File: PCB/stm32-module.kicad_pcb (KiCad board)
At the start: 4 copper layers, 70.2 x 87.4 mm, 24 parts, among them J1 Left, J2 Right

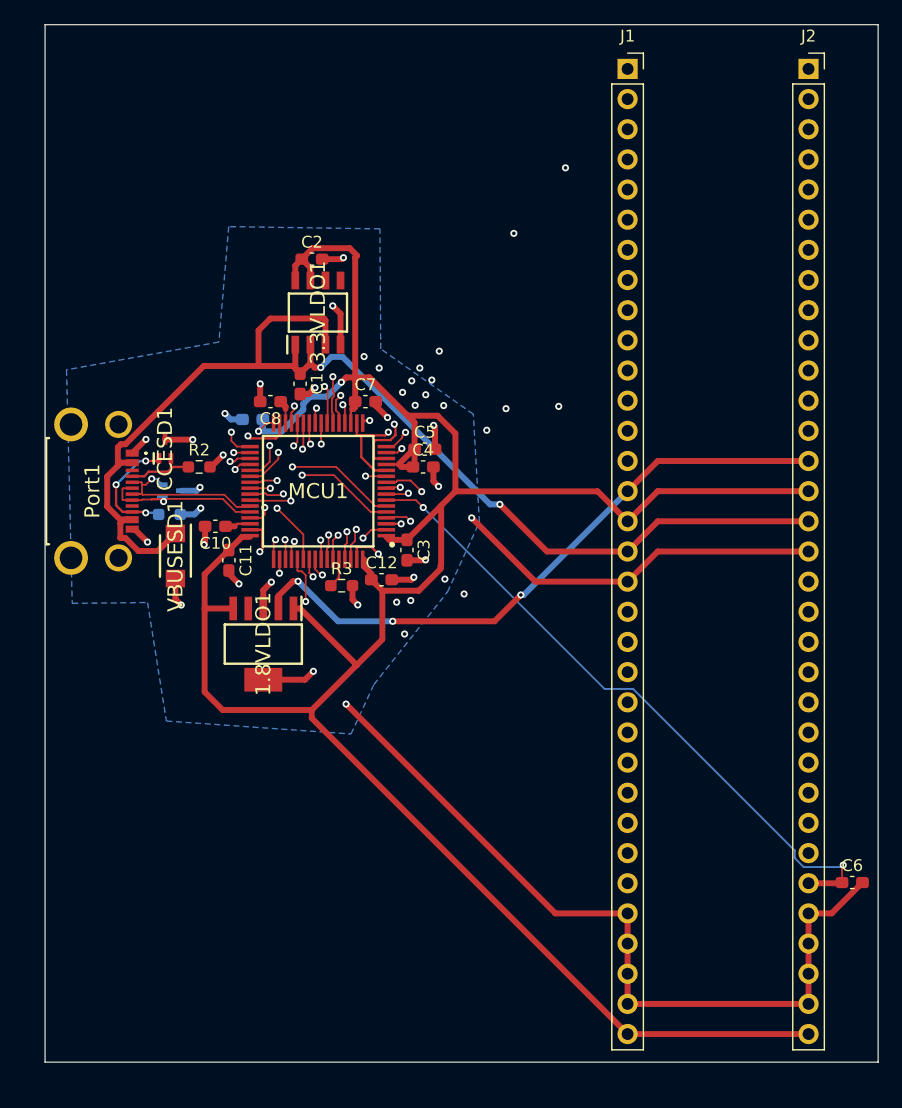
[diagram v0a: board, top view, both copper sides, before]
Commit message: Added images to rom, also rerouted everything
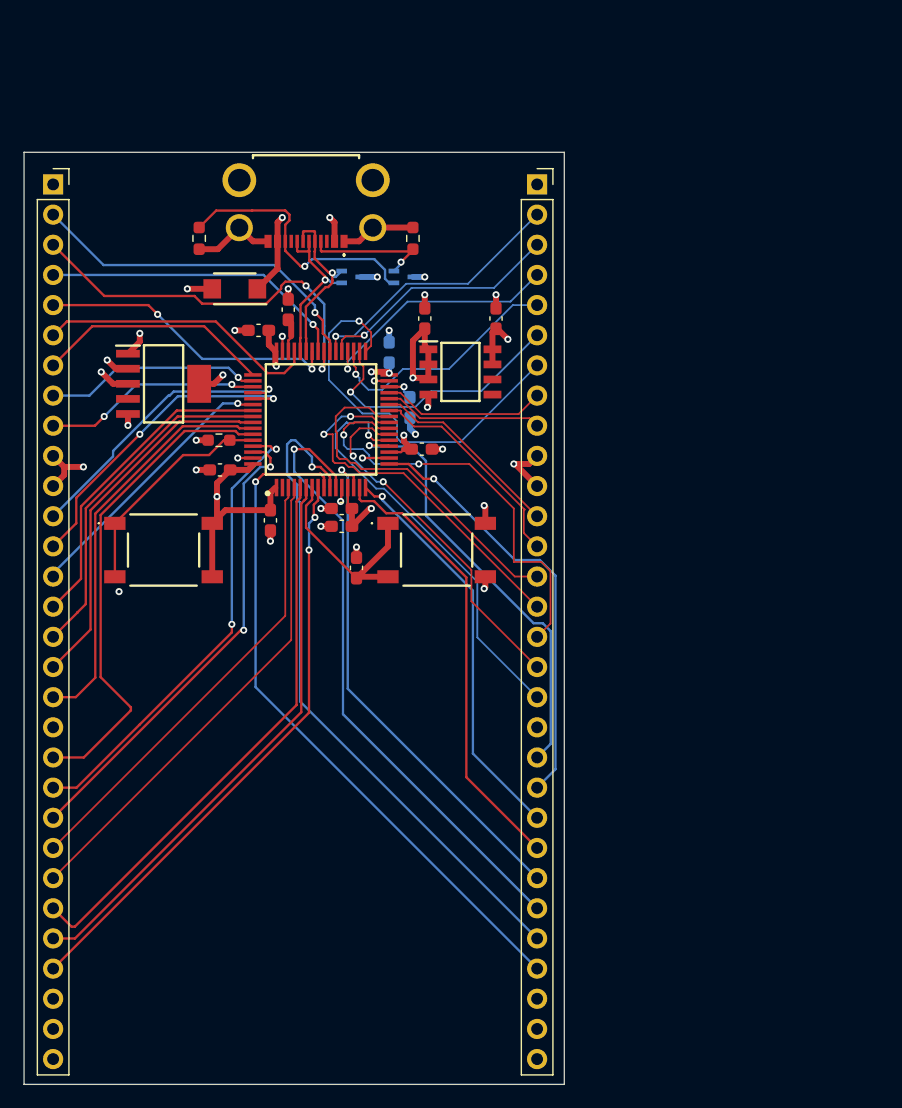
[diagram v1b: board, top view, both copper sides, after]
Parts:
- added S1: TS40-66-43-BK-160-SMT-TR, REQUIRED:TS406643BK160SMTTR, F.Cu at (116.0, 71.0)
- added S2: TS40-66-43-BK-160-SMT-TR, REQUIRED:TS406643BK160SMTTR, F.Cu at (93.0, 71.0)
- 1.8VLDO1: footprint SamacSys_Parts:SOT127P706X180-6N -> REQUIRED:SOT127P706X180-6N
- 3.3VLDO1: footprint SamacSys_Parts:SOIC127P600X175-8N -> REQUIRED:SOIC127P600X175-8N
- C1, C10, C11, C12, C2, C3, C4, C5, C6, C7, C9: footprint Capacitor_SMD:C_0603_1608Metric_Pad1.08x0.95mm_HandSolder -> REQUIRED:C_0603_1608Metric_Pad1.08x0.95mm_HandSolder
- C8: footprint Capacitor_SMD:C_0603_1608Metric_Pad1.08x0.95mm_HandSolder -> REQUIRED:C_0603_1608Metric_Pad1.08x0.95mm_HandSolder; moved to B.Cu
- CCESD1: footprint SamacSys_Parts:SOT50P160X90-3N -> REQUIRED:SOT50P160X90-3N; moved to B.Cu
- DATAESD1: footprint SamacSys_Parts:SOT50P160X90-3N -> REQUIRED:SOT50P160X90-3N
- J1: value Left -> Conn_01x30_Socket; footprint Connector_PinSocket_2.54mm:PinSocket_1x33_P2.54mm_Vertical -> REQUIRED:PinSocket_1x30_P2.54mm_Vertical
- J2: value Right -> Conn_01x30_Socket; footprint Connector_PinSocket_2.54mm:PinSocket_1x33_P2.54mm_Vertical -> REQUIRED:PinSocket_1x30_P2.54mm_Vertical
- MCU1: footprint SamacSys_Parts:QFP50P1200X1200X160-64N -> REQUIRED:QFP50P1200X1200X160-64N
- Port1: footprint SamacSys_Parts:2169900003 -> REQUIRED:2169900003
- R1: footprint Resistor_SMD:R_0603_1608Metric_Pad0.98x0.95mm_HandSolder -> REQUIRED:R_0603_1608Metric_Pad0.98x0.95mm_HandSolder; moved to F.Cu
- R2, R3: footprint Resistor_SMD:R_0603_1608Metric_Pad0.98x0.95mm_HandSolder -> REQUIRED:R_0603_1608Metric_Pad0.98x0.95mm_HandSolder
- VBUSESD1: footprint SamacSys_Parts:SODFL4626X140N -> REQUIRED:SODFL4626X140N
- moved C6 49.5 mm to (109.2, 72.5), turned to 90 degrees
- moved J1 49.3 mm to (83.7, 40.2)
- moved Port1 31.2 mm to (105.0, 41.0), turned to 180 degrees
- moved R2 26.4 mm to (114.0, 44.8), turned to 90 degrees
- moved J2 24.8 mm to (124.5, 40.2)
- moved CCESD1 24.8 mm to (113.2, 48.0), turned to 0 degrees
- moved DATAESD1 23.5 mm to (108.8, 48.0)
- moved 1.8VLDO1 23.5 mm to (93.0, 57.0), turned to 0 degrees
- moved R1 23.4 mm to (96.0, 44.8), turned to -90 degrees
- moved VBUSESD1 23.0 mm to (99.0, 49.0), turned to 180 degrees
- moved C11 19.5 mm to (101.0, 52.5), turned to 180 degrees
- moved C10 19.3 mm to (103.5, 50.8), turned to 90 degrees
- moved C12 16.5 mm to (97.8, 64.2), turned to 180 degrees
- moved C2 16.3 mm to (121.0, 51.5), turned to 90 degrees
- moved R3 16.0 mm to (97.7, 61.8), turned to 180 degrees
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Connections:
- net Net-(MCU1-BOOT0) renamed /BOOT0
- J1 pad 1: /PA0 -> /VBUS
- J1 pad 10: /PA9 -> /1.8V
- J1 pad 11: /PA10 -> /1.8V
- J1 pad 12: /PA13 -> /PC11
- J1 pad 13: /PA14 -> /PC12
- J1 pad 14: /PA15 -> /PD2
- J1 pad 15: /1.8V -> /PB3
- J1 pad 16: /VDDA -> /PB4
- J1 pad 17: /VBUS -> /PB5
- J1 pad 18: GND -> /PB6
- J1 pad 19: /PB0 -> GND
- J1 pad 2: /PA1 -> /PC9
- J1 pad 20: /PB1 -> /PB7
- J1 pad 21: /PB2 -> /PB8
- J1 pad 22: /PB3 -> /PB9
- J1 pad 23: /PB4 -> /PC14
- J1 pad 24: /PB5 -> /PC15
- J1 pad 25: /PB6 -> /PH0
- J1 pad 26: /PB7 -> /PH1
- J1 pad 27: /PB8 -> /PC0
- J1 pad 28: /PB9 -> GND
- J1 pad 3: /PA2 -> /PA8
- J1 pad 4: /PA3 -> /PA9
- J1 pad 5: /PA4 -> /PA10
- J1 pad 6: /PA5 -> /PA13
- J1 pad 7: /PA6 -> /PA14
- J1 pad 8: /PA7 -> /PA15
- J1 pad 9: /PA8 -> /PC10
- J2 pad 1: /PB10 -> /VBUS
- J2 pad 10: /PC4 -> /VDDA
- J2 pad 11: /PC5 -> /VDDA
- J2 pad 12: /PC6 -> /PB1
- J2 pad 13: /PC7 -> /PB0
- J2 pad 14: /1.8V -> /PC5
- J2 pad 15: /VDDA -> /PC4
- J2 pad 16: /VBUS -> /PA7
- J2 pad 17: GND -> /PA6
- J2 pad 18: /PC9 -> /PA5
- J2 pad 19: /PC10 -> GND
- J2 pad 2: /PB12 -> /PC7
- J2 pad 20: /PC11 -> /PA4
- J2 pad 21: /PC12 -> /PA3
- J2 pad 22: /PC13 -> /PA2
- J2 pad 23: /PC14 -> /PA1
- J2 pad 24: /PC15 -> /PA0
- J2 pad 25: /PD2 -> /PC3
- J2 pad 26: /PH0 -> /PC2
- J2 pad 27: /PH1 -> /PC1
- J2 pad 28: /NRST -> GND
- J2 pad 3: /PB13 -> /PC6
- J2 pad 4: /PB14 -> /PB15
- J2 pad 5: /PB15 -> /PB14
- J2 pad 6: /PC0 -> /PB13
- J2 pad 7: /PC1 -> /PB12
- J2 pad 8: /PC2 -> /PB10
- J2 pad 9: /PC3 -> /PB2
- MCU1 pad 2: /PC13 -> unconnected-(MCU1-PC13-Pad2)
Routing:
- net /VDDA: track 215.1 -> 132.9 mm, vias 2 -> 10
- net /PB14: track 83.0 -> 20.9 mm
- net /PC7: track 82.3 -> 22.5 mm, vias 4 -> 1
- net /PB13: track 77.1 -> 22.8 mm
- net /PC6: track 70.8 -> 20.7 mm, vias 2 -> 1
- net /PC13: track 49.4 -> 0.00 mm, vias 2 -> 0
- net /PB10: track 58.0 -> 13.8 mm, vias 1 -> 0
- net /PD2: track 65.1 -> 23.1 mm
- net /PC11: track 64.9 -> 24.3 mm
- net /PB15: track 61.1 -> 21.1 mm
- net /PB12: track 72.3 -> 33.3 mm
- net /NRST: track 56.1 -> 18.2 mm, vias 2 -> 0
- net /1.8V: track 53.2 -> 17.1 mm, vias 3 -> 2
- net /PC10: track 52.1 -> 18.3 mm, vias 3 -> 2
- net /PH1: track 79.1 -> 47.9 mm, vias 1 -> 0
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- added copper zone on In2.Cu, net GND
- removed copper zone on B.Cu, net GND
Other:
- board size 70.2 x 87.4 mm -> 45.5 x 78.5 mm

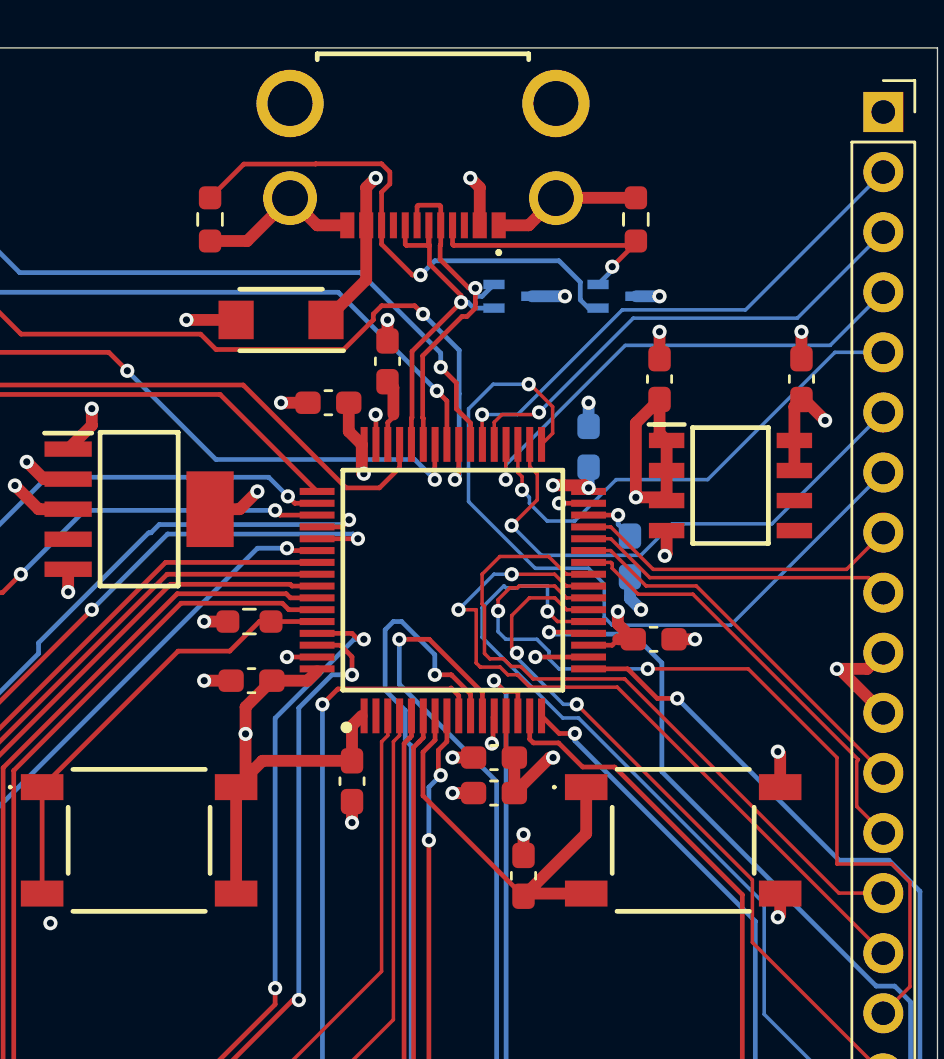
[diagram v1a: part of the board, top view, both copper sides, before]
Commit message: Changed readme, pcb and schematic to reflect different connector chosen due to availability
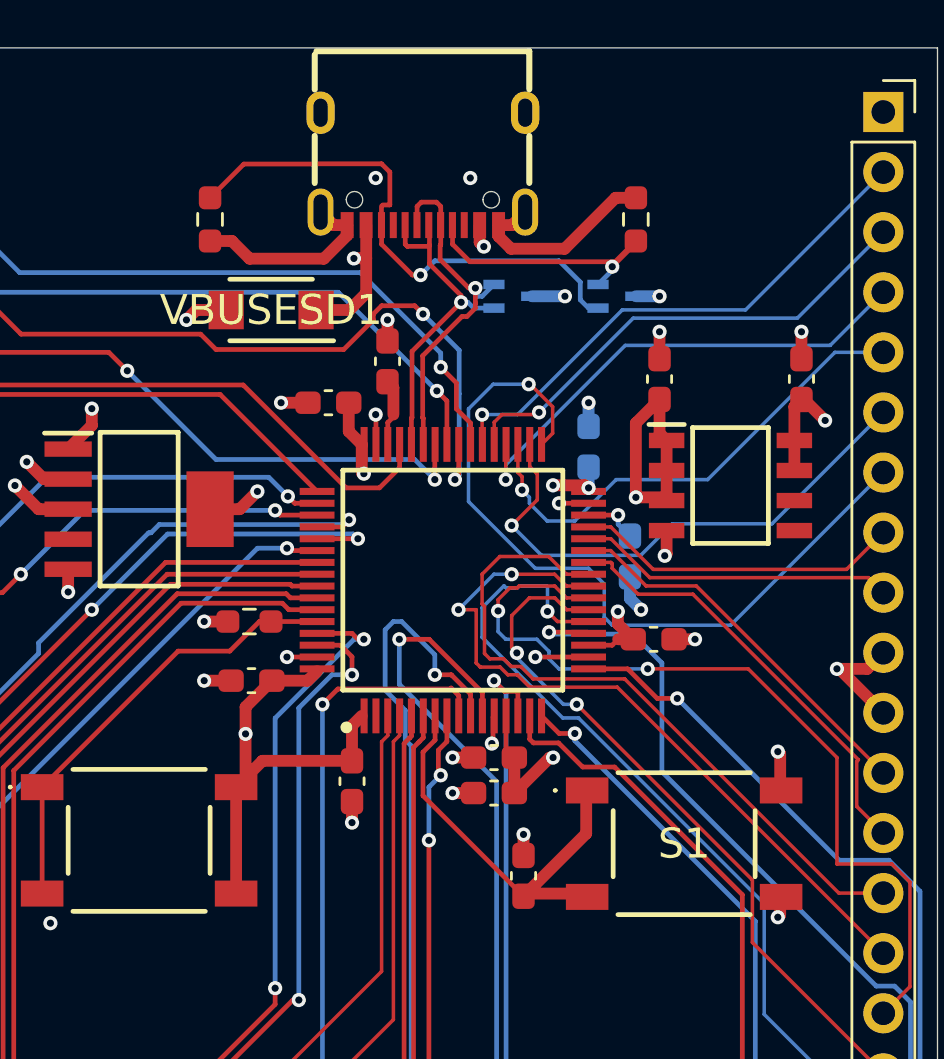
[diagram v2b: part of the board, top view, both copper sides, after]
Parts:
- removed Port1: 216990-0003, REQUIRED:2169900003
- added USB1: ~, REQUIRED:conn, F.Cu at (105.0, 42.6)
- 1.8VLDO1: footprint REQUIRED:SOT127P706X180-6N -> SamacSys_Parts:SOT127P706X180-6N
- 3.3VLDO1: footprint REQUIRED:SOIC127P600X175-8N -> SamacSys_Parts:SOIC127P600X175-8N
- C1, C10, C11, C12, C2, C3, C4, C5, C6, C7, C8, C9: footprint REQUIRED:C_0603_1608Metric_Pad1.08x0.95mm_HandSolder -> Capacitor_SMD:C_0603_1608Metric_Pad1.08x0.95mm_HandSolder
- CCESD1, DATAESD1: footprint REQUIRED:SOT50P160X90-3N -> SamacSys_Parts:SOT50P160X90-3N
- J1, J2: footprint REQUIRED:PinSocket_1x30_P2.54mm_Vertical -> Connector_PinSocket_2.54mm:PinSocket_1x30_P2.54mm_Vertical
- MCU1: footprint REQUIRED:QFP50P1200X1200X160-64N -> SamacSys_Parts:QFP50P1200X1200X160-64N
- R1, R2, R3: footprint REQUIRED:R_0603_1608Metric_Pad0.98x0.95mm_HandSolder -> Resistor_SMD:R_0603_1608Metric_Pad0.98x0.95mm_HandSolder
- S1, S2: value TS40-66-43-BK-160-SMT-TR -> SHOU HAN TS6643TP 250gf 009; footprint REQUIRED:TS406643BK160SMTTR -> SamacSys_Parts:TS406643BK160SMTTR
- VBUSESD1: footprint REQUIRED:SODFL4626X140N -> SamacSys_Parts:SODFL4626X140N
- moved VBUSESD1 0.59 mm to (98.6, 48.6)
- moved S1 0.15 mm to (116.0, 71.1)
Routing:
- net /VBUS: track 81.9 -> 91.8 mm, vias 3 -> 5
- net GND: track 152.5 -> 156.3 mm
- net /D+: track 14.8 -> 14.1 mm
- net /CC1: track 11.1 -> 11.7 mm

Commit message: Added connector footprint with 3d model
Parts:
- removed USB1: ~, REQUIRED:conn
- added J3: TYPE-C_16PIN_2MD__073_, REQUIRED:SHOUHAN_TYPE-C_16PIN_2MD__073_, F.Cu at (105.0, 41.3)
- 1.8VLDO1: footprint SamacSys_Parts:SOT127P706X180-6N -> REQUIRED:SOT127P706X180-6N
- 3.3VLDO1: footprint SamacSys_Parts:SOIC127P600X175-8N -> REQUIRED:SOIC127P600X175-8N
- C1, C10, C11, C12, C2, C3, C4, C5, C6, C7, C8, C9: footprint Capacitor_SMD:C_0603_1608Metric_Pad1.08x0.95mm_HandSolder -> REQUIRED:C_0603_1608Metric_Pad1.08x0.95mm_HandSolder
- CCESD1, DATAESD1: footprint SamacSys_Parts:SOT50P160X90-3N -> REQUIRED:SOT50P160X90-3N
- J1, J2: footprint Connector_PinSocket_2.54mm:PinSocket_1x30_P2.54mm_Vertical -> REQUIRED:PinSocket_1x30_P2.54mm_Vertical
- MCU1: footprint SamacSys_Parts:QFP50P1200X1200X160-64N -> REQUIRED:QFP50P1200X1200X160-64N
- R1, R2, R3: footprint Resistor_SMD:R_0603_1608Metric_Pad0.98x0.95mm_HandSolder -> REQUIRED:R_0603_1608Metric_Pad0.98x0.95mm_HandSolder
- S1, S2: footprint SamacSys_Parts:TS406643BK160SMTTR -> REQUIRED:TS406643BK160SMTTR
- VBUSESD1: footprint SamacSys_Parts:SODFL4626X140N -> REQUIRED:SODFL4626X140N
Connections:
- net /VDDA renamed +3.3V

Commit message: Added hat pins
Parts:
- added REF**: PinHeader_1x01_P2.54mm_Vertical, Connector_PinHeader_2.54mm:PinHeader_1x01_P2.54mm_Vertical, F.Cu at (104.1, 111.8)
- added REF**: PinHeader_1x01_P2.54mm_Vertical, Connector_PinHeader_2.54mm:PinHeader_1x01_P2.54mm_Vertical, F.Cu at (104.1, 101.6)
- added REF**: PinHeader_1x01_P2.54mm_Vertical, Connector_PinHeader_2.54mm:PinHeader_1x01_P2.54mm_Vertical, F.Cu at (99.1, 106.7)
- added REF**: PinHeader_1x01_P2.54mm_Vertical, Connector_PinHeader_2.54mm:PinHeader_1x01_P2.54mm_Vertical, F.Cu at (99.1, 111.8)
- added REF**: PinHeader_1x01_P2.54mm_Vertical, Connector_PinHeader_2.54mm:PinHeader_1x01_P2.54mm_Vertical, F.Cu at (109.2, 111.8)
- added REF**: PinHeader_1x01_P2.54mm_Vertical, Connector_PinHeader_2.54mm:PinHeader_1x01_P2.54mm_Vertical, F.Cu at (109.2, 106.7)
- added REF**: PinHeader_1x01_P2.54mm_Vertical, Connector_PinHeader_2.54mm:PinHeader_1x01_P2.54mm_Vertical, F.Cu at (99.1, 101.6)
- added REF**: PinHeader_1x01_P2.54mm_Vertical, Connector_PinHeader_2.54mm:PinHeader_1x01_P2.54mm_Vertical, F.Cu at (109.2, 101.6)
- added REF**: PinHeader_1x01_P2.54mm_Vertical, Connector_PinHeader_2.54mm:PinHeader_1x01_P2.54mm_Vertical, F.Cu at (104.1, 106.7)
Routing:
- net (no net): vias 0 -> 9
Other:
- board text added: "HAT PINS"

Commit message: Corrected button wiring
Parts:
- removed S1, S2: SHOU HAN TS6643TP 250gf 009, REQUIRED:TS406643BK160SMTTR
- added BOOT_BUTTON1: TS6643TP 250GF 009, REQUIRED:SW-SMD_4P-L6.2-W6.0-P4.50-LS9.0, F.Cu at (93.0, 71.0)
- added RESET_BUTTON1: TS6643TP 250GF 009, REQUIRED:SW-SMD_4P-L6.2-W6.0-P4.50-LS9.0, F.Cu at (116.0, 71.1)
- REF** (x9): footprint Connector_PinHeader_2.54mm:PinHeader_1x01_P2.54mm_Vertical -> REQUIRED:PinHeader_1x01_P2.54mm_Vertical
- turned R3 to 0 degrees
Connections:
- R3 pad 1: /BOOT0 -> GND
- R3 pad 2: GND -> /BOOT0
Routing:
- net +3.3V: track 132.9 -> 141.3 mm
- net /NRST: track 18.2 -> 22.5 mm, vias 0 -> 2
- net /BOOT0: track 19.0 -> 21.8 mm
- net GND: track 156.3 -> 157.7 mm, vias 27 -> 28

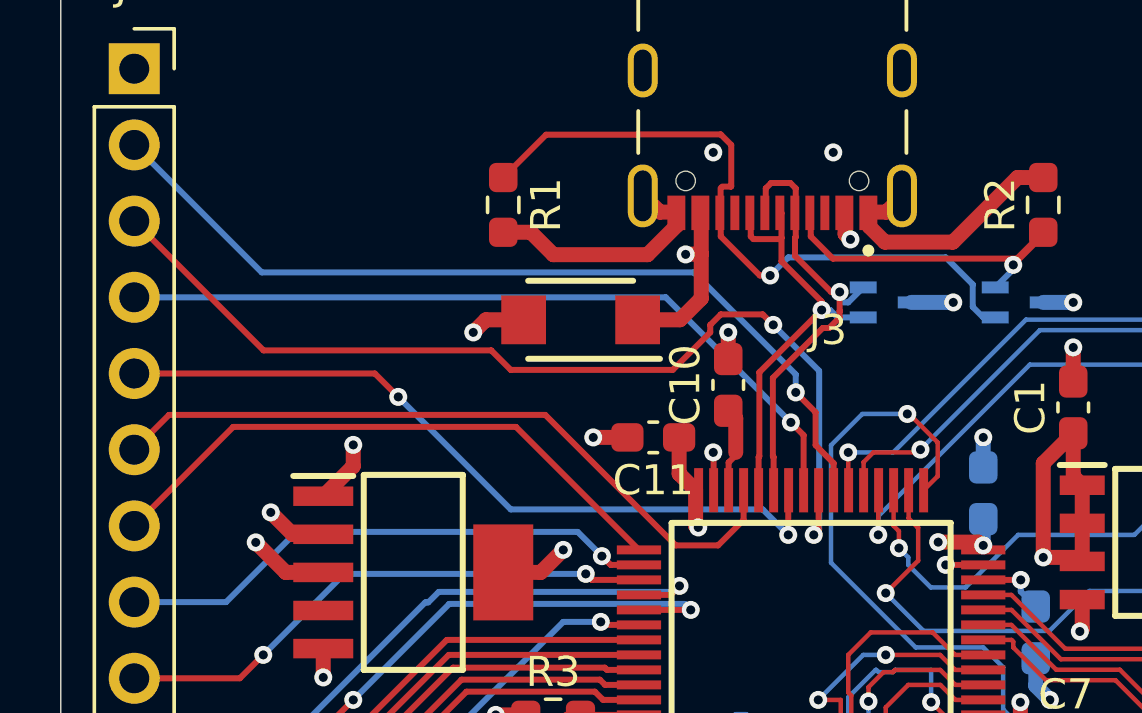
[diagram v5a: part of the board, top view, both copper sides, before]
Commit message: delay tuned usb pair
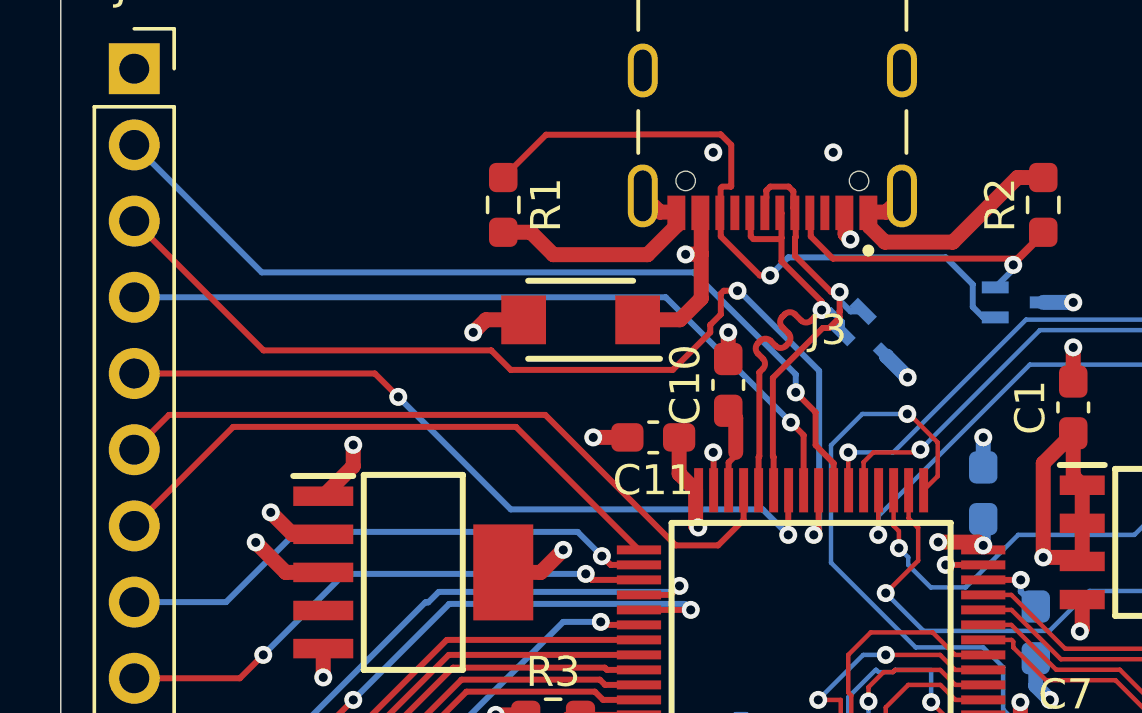
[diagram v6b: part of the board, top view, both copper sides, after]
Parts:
- moved DATAESD1 1.36 mm to (108.2, 49.2), turned to -45 degrees
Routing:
- net /D+: track 14.1 -> 15.9 mm
- net /PA8: track 33.7 -> 34.7 mm
